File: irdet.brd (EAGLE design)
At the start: 50 x 45 mm, 70 parts, among them IC1 MEGA8-AI, IC2 78L05F, IC3 78L08F, J1 PSH02-04WG, J2 PSH02-04WG, J3 PSH02-04WG, J4 PSH02-04WG, J5 22-05-7098-09, T1 BC847, T2 BC857, T3 BC847, T4 BC857, T5 BC847, T6 BC857, T7 BC847, T8 BC857, X1 MVE252-5-V, X2 MVE252-5-V

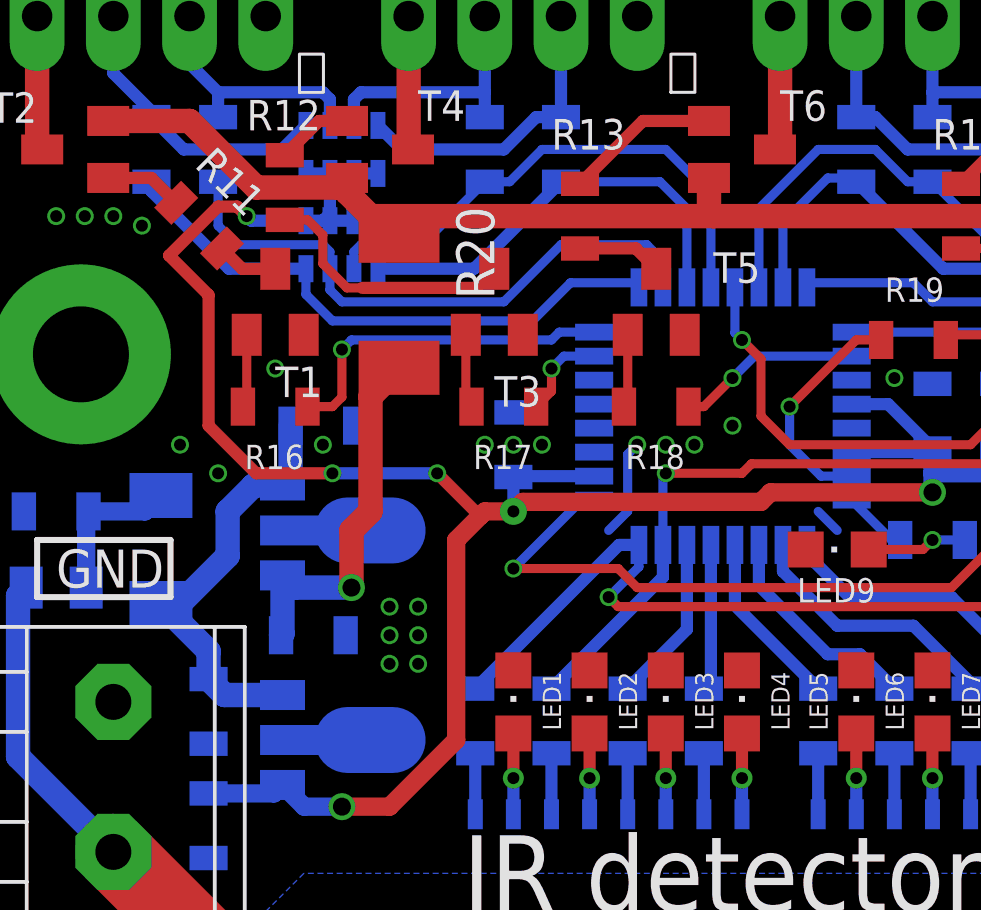
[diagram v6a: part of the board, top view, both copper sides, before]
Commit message: Make silkscreen nice.
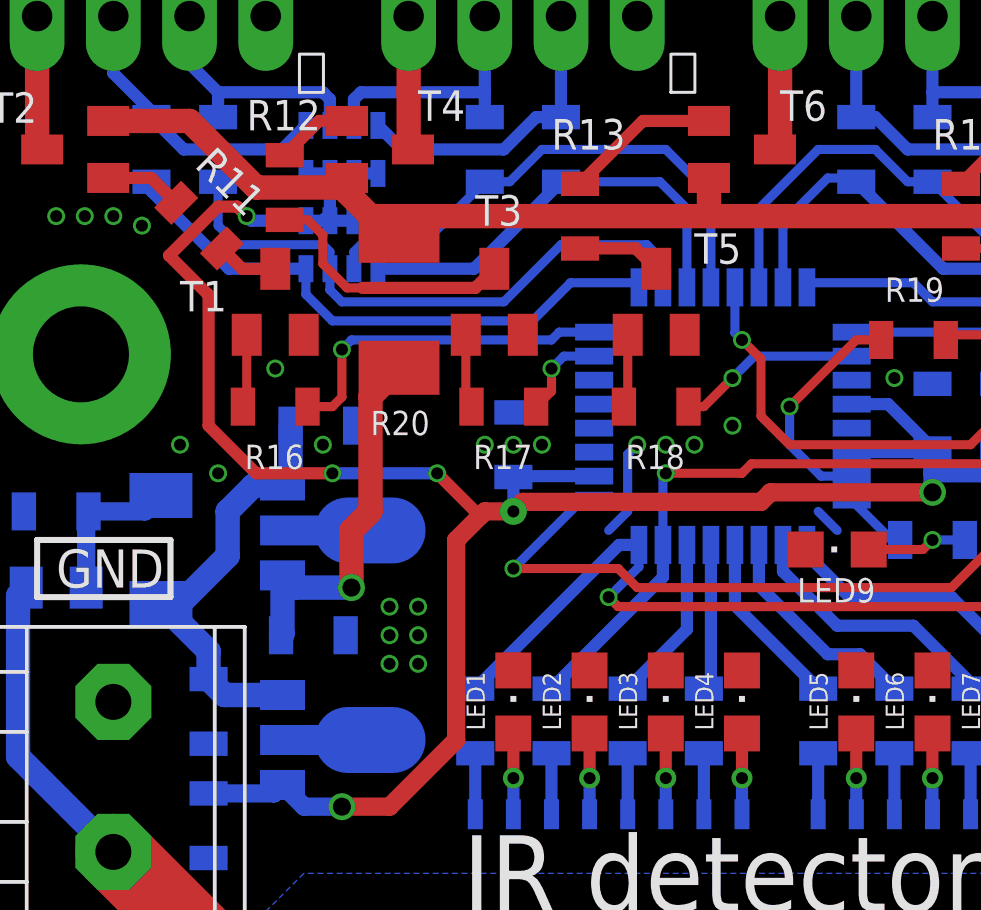
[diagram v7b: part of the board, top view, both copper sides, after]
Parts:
- R20: value 68R -> 47R
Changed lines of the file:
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@@
 <element name="C16" library="rcl" package="C0805" value="22u" x="12.065" y="27.6225" smashed="yes" rot="MR180">
 <attribute name="LCSC_PART" value="C45783" x="12.065" y="27.6225" size="1.778" layer="28" rot="MR180" display="off"/>
-<attribute name="NAME" x="13.97" y="27.305" size="1.016" layer="26" rot="MR90"/>
+<attribute name="NAME" x="13.335" y="28.575" size="1.016" layer="26" rot="MR0"/>
 <attribute name="VALUE" x="10.795" y="26.67" size="1.016" layer="28" rot="MR180"/>
 </element>
@@
 <element name="D3" library="diode" library_urn="urn:adsk.eagle:library:210" package="SOD-123_MINI-SMA" package3d_urn="urn:adsk.eagle:package:43457/2" value="SM4007PL" x="6.6675" y="23.495" smashed="yes" rot="MR90">
 <attribute name="LCSC_PART" value="C64898" x="6.6675" y="23.495" size="1.778" layer="28" rot="MR90" display="off"/>
-<attribute name="NAME" x="7.493" y="19.558" size="1.016" layer="26" rot="MR0"/>
+<attribute name="NAME" x="8.128" y="26.543" size="1.016" layer="26" rot="MR0"/>
 <attribute name="POPULARITY" value="0" x="-56.8325" y="89.535" size="1.778" layer="28" rot="MR90" display="off"/>
 <attribute name="VALUE" x="7.4295" y="26.162" size="1.016" layer="28" rot="MR90"/>
@@
 </element>
 <element name="LED1" library="led" library_urn="urn:adsk.eagle:library:259" package="CHIPLED_0805" package3d_urn="urn:adsk.eagle:package:15821/2" value="YEL" x="18.415" y="18.415" smashed="yes">
-<attribute name="NAME" x="20.0025" y="17.4625" size="0.6096" layer="25" rot="R90"/>
+<attribute name="NAME" x="17.4625" y="17.4625" size="0.6096" layer="25" rot="R90"/>
 <attribute name="POPULARITY" value="52" x="61.595" y="-50.165" size="1.778" layer="27" display="off"/>
 <attribute name="VALUE" x="20.955" y="17.145" size="1.27" layer="27" rot="R90"/>
 </element>
 <element name="LED2" library="led" library_urn="urn:adsk.eagle:library:259" package="CHIPLED_0805" package3d_urn="urn:adsk.eagle:package:15821/2" value="YEL" x="20.955" y="18.415" smashed="yes">
-<attribute name="NAME" x="22.5425" y="17.4625" size="0.6096" layer="25" rot="R90"/>
+<attribute name="NAME" x="20.0025" y="17.4625" size="0.6096" layer="25" rot="R90"/>
 <attribute name="POPULARITY" value="52" x="69.215" y="-50.165" size="1.778" layer="27" display="off"/>
 <attribute name="VALUE" x="23.495" y="17.145" size="1.27" layer="27" rot="R90"/>
 </element>
 <element name="LED3" library="led" library_urn="urn:adsk.eagle:library:259" package="CHIPLED_0805" package3d_urn="urn:adsk.eagle:package:15821/2" value="YEL" x="23.495" y="18.415" smashed="yes">
-<attribute name="NAME" x="25.0825" y="17.4625" size="0.6096" layer="25" rot="R90"/>
+<attribute name="NAME" x="22.5425" y="17.4625" size="0.6096" layer="25" rot="R90"/>
 <attribute name="POPULARITY" value="52" x="76.835" y="-50.165" size="1.778" layer="27" display="off"/>
 <attribute name="VALUE" x="26.035" y="17.145" size="1.27" layer="27" rot="R90"/>
 </element>
 <element name="LED4" library="led" library_urn="urn:adsk.eagle:library:259" package="CHIPLED_0805" package3d_urn="urn:adsk.eagle:package:15821/2" value="YEL" x="26.035" y="18.415" smashed="yes">
-<attribute name="NAME" x="27.6225" y="17.4625" size="0.6096" layer="25" rot="R90"/>
+<attribute name="NAME" x="25.0825" y="17.4625" size="0.6096" layer="25" rot="R90"/>
 <attribute name="POPULARITY" value="52" x="84.455" y="-50.165" size="1.778" layer="27" display="off"/>
 <attribute name="VALUE" x="28.575" y="17.145" size="1.27" layer="27" rot="R90"/>
@@
 </element>
 <element name="T1" library="transistor" library_urn="urn:adsk.eagle:library:402" package="SOT23-BEC" package3d_urn="urn:adsk.eagle:package:28748/2" value="BC847" x="10.4775" y="31.75" smashed="yes">
-<attribute name="NAME" x="10.4775" y="28.575" size="1.016" layer="25"/>
+<attribute name="NAME" x="7.3025" y="31.4325" size="1.016" layer="25"/>
 <attribute name="POPULARITY" value="0" x="63.8175" y="-7.62" size="1.778" layer="27" display="off"/>
 <attribute name="VALUE" x="8.255" y="28.8925" size="1.016" layer="27"/>
@@
 </element>
 <element name="T3" library="transistor" library_urn="urn:adsk.eagle:library:402" package="SOT23-BEC" package3d_urn="urn:adsk.eagle:package:28748/2" value="BC847" x="17.78" y="31.75" smashed="yes">
-<attribute name="NAME" x="17.78" y="28.2575" size="1.016" layer="25"/>
+<attribute name="NAME" x="17.145" y="34.29" size="1.016" layer="25"/>
 <attribute name="POPULARITY" value="0" x="83.82" y="-7.62" size="1.778" layer="27" display="off"/>
 <attribute name="VALUE" x="18.0975" y="29.845" size="1.016" layer="27" rot="R270"/>
@@
 </element>
 <element name="T5" library="transistor" library_urn="urn:adsk.eagle:library:402" package="SOT23-BEC" package3d_urn="urn:adsk.eagle:package:28748/2" value="BC847" x="23.1775" y="31.75" smashed="yes">
-<attribute name="NAME" x="25.0825" y="32.385" size="1.016" layer="25"/>
+<attribute name="NAME" x="24.4475" y="33.02" size="1.016" layer="25"/>
 <attribute name="POPULARITY" value="0" x="39.6875" y="-17.78" size="1.778" layer="27" display="off"/>
 <attribute name="VALUE" x="25.0825" y="31.75" size="1.016" layer="27"/>
@@
 <element name="IC3" library="linear" library_urn="urn:adsk.eagle:library:262" package="SOT89" package3d_urn="urn:adsk.eagle:package:16478/2" value="78L08F" x="12.7" y="24.13" smashed="yes" rot="MR90">
 <attribute name="LCSC_PART" value="C122846" x="12.7" y="24.13" size="1.778" layer="28" rot="MR90" display="off"/>
-<attribute name="NAME" x="15.875" y="21.59" size="1.27" layer="26" rot="MR90"/>
+<attribute name="NAME" x="16.1925" y="23.1775" size="1.016" layer="26" rot="MR90"/>
 <attribute name="POPULARITY" value="0" x="12.7" y="24.13" size="1.778" layer="28" rot="MR90" display="off"/>
 <attribute name="VALUE" x="8.3551" y="21.7249" size="1.27" layer="28" rot="MR90"/>
@@
 <element name="C3" library="rcl" package="C0805" value="22u" x="11.7475" y="20.6375" smashed="yes" rot="MR180">
 <attribute name="LCSC_PART" value="C45783" x="11.7475" y="20.6375" size="1.778" layer="28" rot="MR180" display="off"/>
-<attribute name="NAME" x="10.4775" y="19.3675" size="1.27" layer="26" rot="MR180"/>
+<attribute name="NAME" x="8.255" y="21.2725" size="1.016" layer="26" rot="MR180"/>
 <attribute name="VALUE" x="10.4775" y="23.1775" size="1.27" layer="28" rot="MR180"/>
 </element>
-<element name="R20" library="rcl" library_urn="urn:adsk.eagle:library:334" package="R2010" package3d_urn="urn:adsk.eagle:package:23551/2" value="68R" x="14.605" y="31.75" smashed="yes" rot="R270">
-<attribute name="NAME" x="16.51" y="34.925" size="1.27" layer="25" rot="R270"/>
+<element name="R20" library="rcl" library_urn="urn:adsk.eagle:library:334" package="R2010" package3d_urn="urn:adsk.eagle:package:23551/2" value="47R" x="14.605" y="31.75" smashed="yes" rot="R270">
+<attribute name="NAME" x="13.6525" y="27.305" size="0.8128" layer="25"/>
 <attribute name="POPULARITY" value="3" x="14.605" y="31.75" size="1.778" layer="27" rot="R270" display="off"/>
 <attribute name="SPICEPREFIX" value="R" x="14.605" y="31.75" size="1.778" layer="27" rot="R270" display="off"/>
